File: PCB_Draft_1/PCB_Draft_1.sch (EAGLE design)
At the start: 17 parts

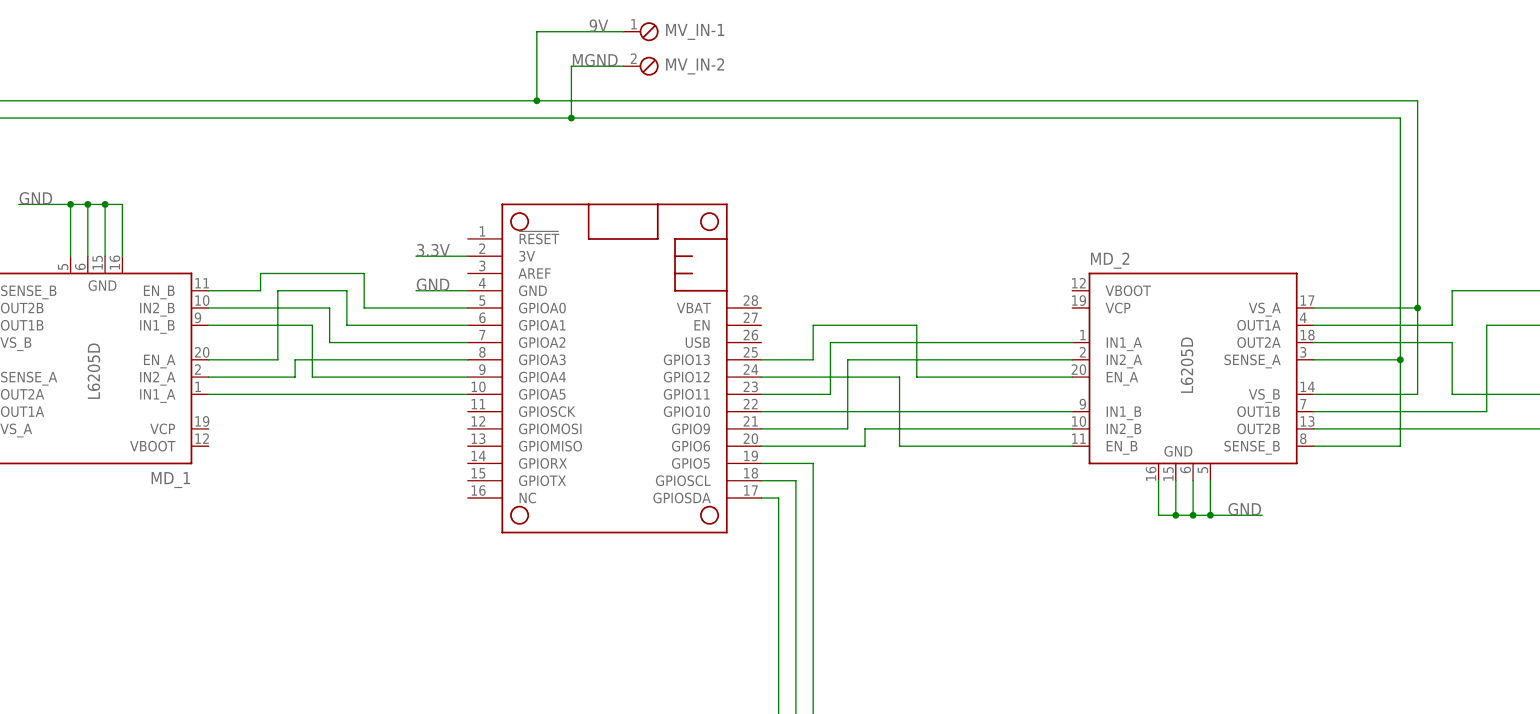
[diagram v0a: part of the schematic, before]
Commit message: Added components for MD bootstrap voltage circuit
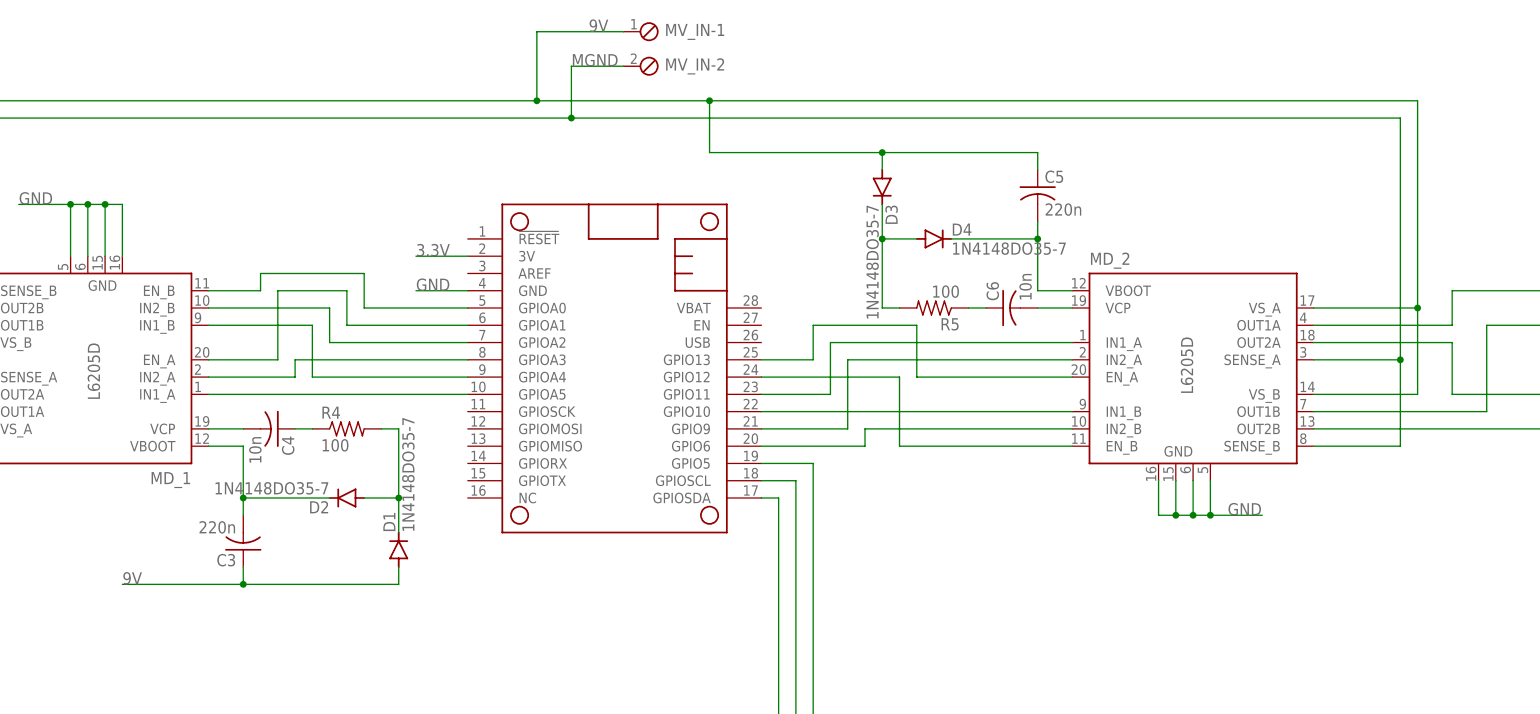
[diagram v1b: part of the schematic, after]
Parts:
- added C3, C5: 220n, rcl:C-USC0805
- added C4, C6: 10n, rcl:C-USC0805
- added D1, D2, D3, D4: 1N4148DO35-7, diode:1N4148DO35-7
- added R4, R5: 100, rcl:R-US_M0805
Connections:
- new net N$18: C4.2, MD_1.VCP
- new net N$25: C4.1, R4.1
- new net N$41: D1.C, D2.A, R4.2
- new net N$42: C3.2, D2.C, MD_1.VBOOT
- new net N$43: C6.2, MD_2.VCP
- new net N$44: C6.1, R5.1
- new net N$45: D3.C, D4.A, R5.2
- new net N$46: C5.2, D4.C, MD_2.VBOOT
- net 9V: now also C3.1, C5.1, D1.A, D3.A
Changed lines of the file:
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@@
 <part name="C2" library="rcl" library_urn="urn:adsk.eagle:library:334" deviceset="C-US" device="C0805" package3d_urn="urn:adsk.eagle:package:23617/2"/>
 <part name="R3" library="rcl" library_urn="urn:adsk.eagle:library:334" deviceset="R-US_" device="M0805" package3d_urn="urn:adsk.eagle:package:23556/2" value="0"/>
+<part name="D1" library="diode" library_urn="urn:adsk.eagle:library:210" deviceset="1N4148" device="DO35-7" package3d_urn="urn:adsk.eagle:package:43339/2"/>
+<part name="D2" library="diode" library_urn="urn:adsk.eagle:library:210" deviceset="1N4148" device="DO35-7" package3d_urn="urn:adsk.eagle:package:43339/2"/>
+<part name="C3" library="rcl" library_urn="urn:adsk.eagle:library:334" deviceset="C-US" device="C0805" package3d_urn="urn:adsk.eagle:package:23617/2" value="220n"/>
+<part name="C4" library="rcl" library_urn="urn:adsk.eagle:library:334" deviceset="C-US" device="C0805" package3d_urn="urn:adsk.eagle:package:23617/2" value="10n"/>
+<part name="R4" library="rcl" library_urn="urn:adsk.eagle:library:334" deviceset="R-US_" device="M0805" package3d_urn="urn:adsk.eagle:package:23556/2" value="100"/>
+<part name="D3" library="diode" library_urn="urn:adsk.eagle:library:210" deviceset="1N4148" device="DO35-7" package3d_urn="urn:adsk.eagle:package:43339/2"/>
+<part name="D4" library="diode" library_urn="urn:adsk.eagle:library:210" deviceset="1N4148" device="DO35-7" package3d_urn="urn:adsk.eagle:package:43339/2"/>
+<part name="C5" library="rcl" library_urn="urn:adsk.eagle:library:334" deviceset="C-US" device="C0805" package3d_urn="urn:adsk.eagle:package:23617/2" value="220n"/>
+<part name="C6" library="rcl" library_urn="urn:adsk.eagle:library:334" deviceset="C-US" device="C0805" package3d_urn="urn:adsk.eagle:package:23617/2" value="10n"/>
+<part name="R5" library="rcl" library_urn="urn:adsk.eagle:library:334" deviceset="R-US_" device="M0805" package3d_urn="urn:adsk.eagle:package:23556/2" value="100"/>
 </parts>
 <sheets>
@@
 <attribute name="NAME" x="105.41" y="54.3814" size="1.778" layer="95" rot="R180"/>
 <attribute name="VALUE" x="105.41" y="59.182" size="1.778" layer="96" rot="R180"/>
+</instance>
+<instance part="D1" gate="G$1" x="167.64" y="162.56" smashed="yes" rot="R90">
+<attribute name="NAME" x="167.1574" y="165.1" size="1.778" layer="95" rot="R90"/>
+<attribute name="VALUE" x="169.9514" y="165.1" size="1.778" layer="96" rot="R90"/>
+</instance>
+<instance part="D2" gate="G$1" x="160.02" y="170.18" smashed="yes" rot="R180">
+<attribute name="NAME" x="157.48" y="169.6974" size="1.778" layer="95" rot="R180"/>
+<attribute name="VALUE" x="157.48" y="172.4914" size="1.778" layer="96" rot="R180"/>
+</instance>
+<instance part="C3" gate="G$1" x="144.78" y="162.56" smashed="yes" rot="R180">
+<attribute name="NAME" x="143.764" y="161.925" size="1.778" layer="95" rot="R180"/>
+<attribute name="VALUE" x="143.764" y="166.751" size="1.778" layer="96" rot="R180"/>
+</instance>
+<instance part="C4" gate="G$1" x="149.86" y="180.34" smashed="yes" rot="R270">
+<attribute name="NAME" x="150.495" y="179.324" size="1.778" layer="95" rot="R270"/>
+<attribute name="VALUE" x="145.669" y="179.324" size="1.778" layer="96" rot="R270"/>
+</instance>
+<instance part="R4" gate="G$1" x="160.02" y="180.34" smashed="yes">
+<attribute name="NAME" x="156.21" y="181.8386" size="1.778" layer="95"/>
+<attribute name="VALUE" x="156.21" y="177.038" size="1.778" layer="96"/>
+</instance>
+<instance part="D3" gate="G$1" x="238.76" y="215.9" smashed="yes" rot="R270">
+<attribute name="NAME" x="239.2426" y="213.36" size="1.778" layer="95" rot="R270"/>
+<attribute name="VALUE" x="236.4486" y="213.36" size="1.778" layer="96" rot="R270"/>
+</instance>
+<instance part="D4" gate="G$1" x="246.38" y="208.28" smashed="yes">
+<attribute name="NAME" x="248.92" y="208.7626" size="1.778" layer="95"/>
+<attribute name="VALUE" x="248.92" y="205.9686" size="1.778" layer="96"/>
+</instance>
+<instance part="C5" gate="G$1" x="261.62" y="215.9" smashed="yes">
+<attribute name="NAME" x="262.636" y="216.535" size="1.778" layer="95"/>
+<attribute name="VALUE" x="262.636" y="211.709" size="1.778" layer="96"/>
+</instance>
+<instance part="C6" gate="G$1" x="256.54" y="198.12" smashed="yes" rot="R90">
+<attribute name="NAME" x="255.905" y="199.136" size="1.778" layer="95" rot="R90"/>
+<attribute name="VALUE" x="260.731" y="199.136" size="1.778" layer="96" rot="R90"/>
+</instance>
+<instance part="R5" gate="G$1" x="246.38" y="198.12" smashed="yes" rot="R180">
+<attribute name="NAME" x="250.19" y="196.6214" size="1.778" layer="95" rot="R180"/>
+<attribute name="VALUE" x="250.19" y="201.422" size="1.778" layer="96" rot="R180"/>
 </instance>
 </instances>
@@
 <wire x1="317.5" y1="185.42" x2="317.5" y2="198.12" width="0.1524" layer="91"/>
 <wire x1="317.5" y1="198.12" x2="317.5" y2="228.6" width="0.1524" layer="91"/>
-<wire x1="317.5" y1="228.6" x2="187.96" y2="228.6" width="0.1524" layer="91"/>
+<wire x1="317.5" y1="228.6" x2="213.36" y2="228.6" width="0.1524" layer="91"/>
+<wire x1="213.36" y1="228.6" x2="187.96" y2="228.6" width="0.1524" layer="91"/>
 <wire x1="187.96" y1="228.6" x2="93.98" y2="228.6" width="0.1524" layer="91"/>
 <wire x1="187.96" y1="228.6" x2="187.96" y2="238.76" width="0.1524" layer="91"/>
@@
 <junction x="317.5" y="198.12"/>
 <label x="195.58" y="238.76" size="1.778" layer="95"/>
+<pinref part="D3" gate="G$1" pin="A"/>
+<wire x1="238.76" y1="218.44" x2="238.76" y2="220.98" width="0.1524" layer="91"/>
+<wire x1="238.76" y1="220.98" x2="261.62" y2="220.98" width="0.1524" layer="91"/>
+<pinref part="C5" gate="G$1" pin="1"/>
+<wire x1="261.62" y1="218.44" x2="261.62" y2="220.98" width="0.1524" layer="91"/>
+<wire x1="213.36" y1="228.6" x2="213.36" y2="220.98" width="0.1524" layer="91"/>
+<wire x1="213.36" y1="220.98" x2="238.76" y2="220.98" width="0.1524" layer="91"/>
+<junction x="213.36" y="228.6"/>
+<junction x="238.76" y="220.98"/>
+</segment>
+<segment>
+<pinref part="D1" gate="G$1" pin="A"/>
+<wire x1="167.64" y1="160.02" x2="167.64" y2="157.48" width="0.1524" layer="91"/>
+<wire x1="167.64" y1="157.48" x2="144.78" y2="157.48" width="0.1524" layer="91"/>
+<pinref part="C3" gate="G$1" pin="1"/>
+<wire x1="144.78" y1="157.48" x2="127" y2="157.48" width="0.1524" layer="91"/>
+<wire x1="144.78" y1="160.02" x2="144.78" y2="157.48" width="0.1524" layer="91"/>
+<junction x="144.78" y="157.48"/>
+<label x="127" y="157.48" size="1.778" layer="95"/>
 </segment>
 </net>
@@
 </segment>
 </net>
+<net name="N$18" class="0">
+<segment>
+<pinref part="MD_1" gate="P1" pin="VCP"/>
+<pinref part="C4" gate="G$1" pin="2"/>
+<wire x1="139.7" y1="180.34" x2="144.78" y2="180.34" width="0.1524" layer="91"/>
+</segment>
+</net>
+<net name="N$25" class="0">
+<segment>
+<pinref part="C4" gate="G$1" pin="1"/>
+<pinref part="R4" gate="G$1" pin="1"/>
+<wire x1="152.4" y1="180.34" x2="154.94" y2="180.34" width="0.1524" layer="91"/>
+</segment>
+</net>
+<net name="N$41" class="0">
+<segment>
+<pinref part="R4" gate="G$1" pin="2"/>
+<wire x1="165.1" y1="180.34" x2="167.64" y2="180.34" width="0.1524" layer="91"/>
+<wire x1="167.64" y1="180.34" x2="167.64" y2="170.18" width="0.1524" layer="91"/>
+<pinref part="D1" gate="G$1" pin="C"/>
+<pinref part="D2" gate="G$1" pin="A"/>
+<wire x1="167.64" y1="170.18" x2="167.64" y2="165.1" width="0.1524" layer="91"/>
+<wire x1="162.56" y1="170.18" x2="167.64" y2="170.18" width="0.1524" layer="91"/>
+<junction x="167.64" y="170.18"/>
+</segment>
+</net>
+<net name="N$42" class="0">
+<segment>
+<pinref part="D2" gate="G$1" pin="C"/>
+<wire x1="157.48" y1="170.18" x2="144.78" y2="170.18" width="0.1524" layer="91"/>
+<wire x1="144.78" y1="170.18" x2="144.78" y2="177.8" width="0.1524" layer="91"/>
+<pinref part="MD_1" gate="P1" pin="VBOOT"/>
+<wire x1="144.78" y1="177.8" x2="139.7" y2="177.8" width="0.1524" layer="91"/>
+<pinref part="C3" gate="G$1" pin="2"/>
+<wire x1="144.78" y1="167.64" x2="144.78" y2="170.18" width="0.1524" layer="91"/>
+<junction x="144.78" y="170.18"/>
+</segment>
+</net>
+<net name="N$43" class="0">
+<segment>
+<pinref part="C6" gate="G$1" pin="2"/>
+<wire x1="266.7" y1="198.12" x2="261.62" y2="198.12" width="0.1524" layer="91"/>
+<pinref part="MD_2" gate="P1" pin="VCP"/>
+</segment>
+</net>
+<net name="N$44" class="0">
+<segment>
+<pinref part="C6" gate="G$1" pin="1"/>
+<pinref part="R5" gate="G$1" pin="1"/>
+<wire x1="254" y1="198.12" x2="251.46" y2="198.12" width="0.1524" layer="91"/>
+</segment>
+</net>
+<net name="N$45" class="0">
+<segment>
+<pinref part="R5" gate="G$1" pin="2"/>
+<wire x1="241.3" y1="198.12" x2="238.76" y2="198.12" width="0.1524" layer="91"/>
+<wire x1="238.76" y1="198.12" x2="238.76" y2="208.28" width="0.1524" layer="91"/>
+<pinref part="D3" gate="G$1" pin="C"/>
+<pinref part="D4" gate="G$1" pin="A"/>
+<wire x1="238.76" y1="208.28" x2="238.76" y2="213.36" width="0.1524" layer="91"/>
+<wire x1="243.84" y1="208.28" x2="238.76" y2="208.28" width="0.1524" layer="91"/>
+<junction x="238.76" y="208.28"/>
+</segment>
+</net>
+<net name="N$46" class="0">
+<segment>
+<pinref part="D4" gate="G$1" pin="C"/>
+<wire x1="248.92" y1="208.28" x2="261.62" y2="208.28" width="0.1524" layer="91"/>
+<wire x1="261.62" y1="208.28" x2="261.62" y2="200.66" width="0.1524" layer="91"/>
+<wire x1="261.62" y1="200.66" x2="266.7" y2="200.66" width="0.1524" layer="91"/>
+<pinref part="C5" gate="G$1" pin="2"/>
+<wire x1="261.62" y1="210.82" x2="261.62" y2="208.28" width="0.1524" layer="91"/>
+<junction x="261.62" y="208.28"/>
+<pinref part="MD_2" gate="P1" pin="VBOOT"/>
+</segment>
+</net>
